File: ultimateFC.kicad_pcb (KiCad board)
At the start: 8 copper layers, 73 parts, among them J1 USB_B_Micro, U14 TPS62824ADMQ, U32 LMR33630CQRNX, U33 STM32H735VGH6, U36 ICM-20602, U37 S25FL064L, U39 BMP280, Y1 CSTNE8M00G550000R0

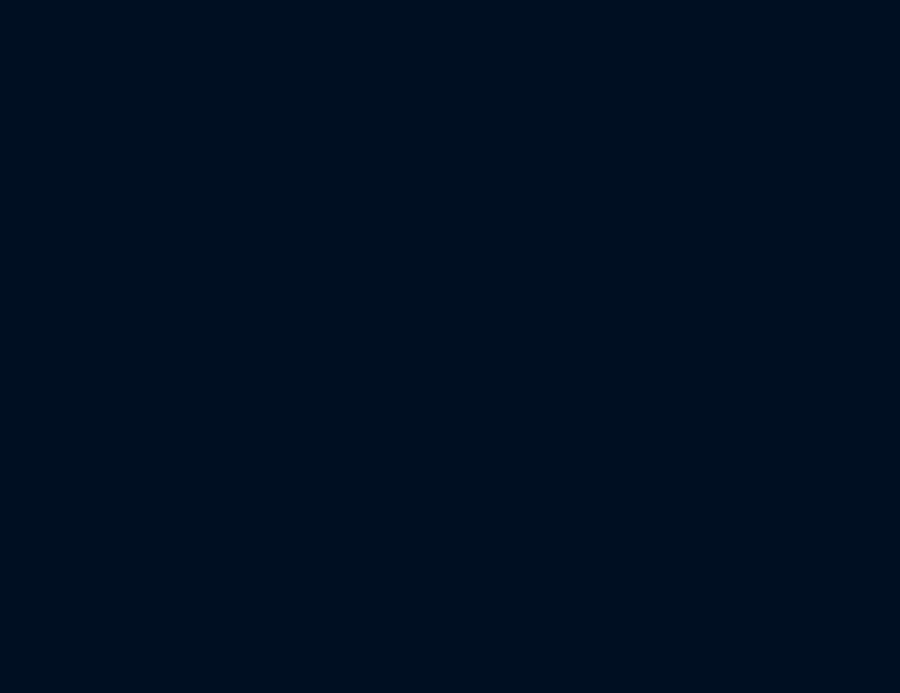
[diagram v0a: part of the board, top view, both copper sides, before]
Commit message: add HD DCDC
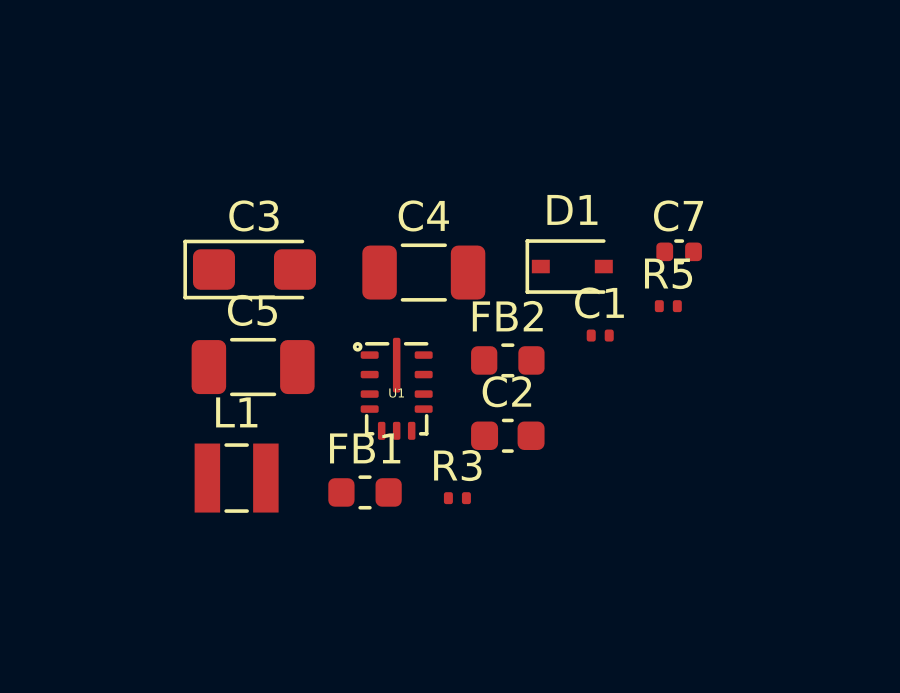
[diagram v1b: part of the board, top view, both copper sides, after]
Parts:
- added C1: 100nF, ultimateFC:C_0201_0603Metric_mod, F.Cu at (155.0, 115.0)
- added C2: 10µF, Capacitor_SMD:C_0603_1608Metric, F.Cu at (151.9, 118.3)
- added C3: 100µF, Capacitor_Tantalum_SMD:CP_EIA-3216-10_Kemet-I, F.Cu at (143.5, 112.8)
- added C4: 10µF, Capacitor_SMD:C_1206_3216Metric, F.Cu at (149.1, 112.9)
- added C5: 10µF, Capacitor_SMD:C_1206_3216Metric, F.Cu at (143.4, 116.0)
- added C7: 1µF, Capacitor_SMD:C_0402_1005Metric, F.Cu at (157.6, 112.2)
- added D1: PMEG3020EJ,115, Diode_SMD:D_SOD-323, F.Cu at (154.1, 112.7)
- added FB1: 120R@100Mhz, Inductor_SMD:L_0603_1608Metric, F.Cu at (147.2, 120.2)
- added FB2: 120R@100Mhz, Inductor_SMD:L_0603_1608Metric, F.Cu at (151.9, 115.8)
- added L1: 1µH, Inductor_SMD:L_Wuerth_MAPI-2506, F.Cu at (142.9, 119.8)
- added R3: 100k, ultimateFC:R_0201_0603Metric_mod, F.Cu at (150.2, 120.4)
- added R5: 11k, ultimateFC:R_0201_0603Metric_mod, F.Cu at (157.3, 114.0)
- added U1: LMR33620CRNXT, ultimateFC:Texas_RNX0012B, F.Cu at (148.2, 116.8)

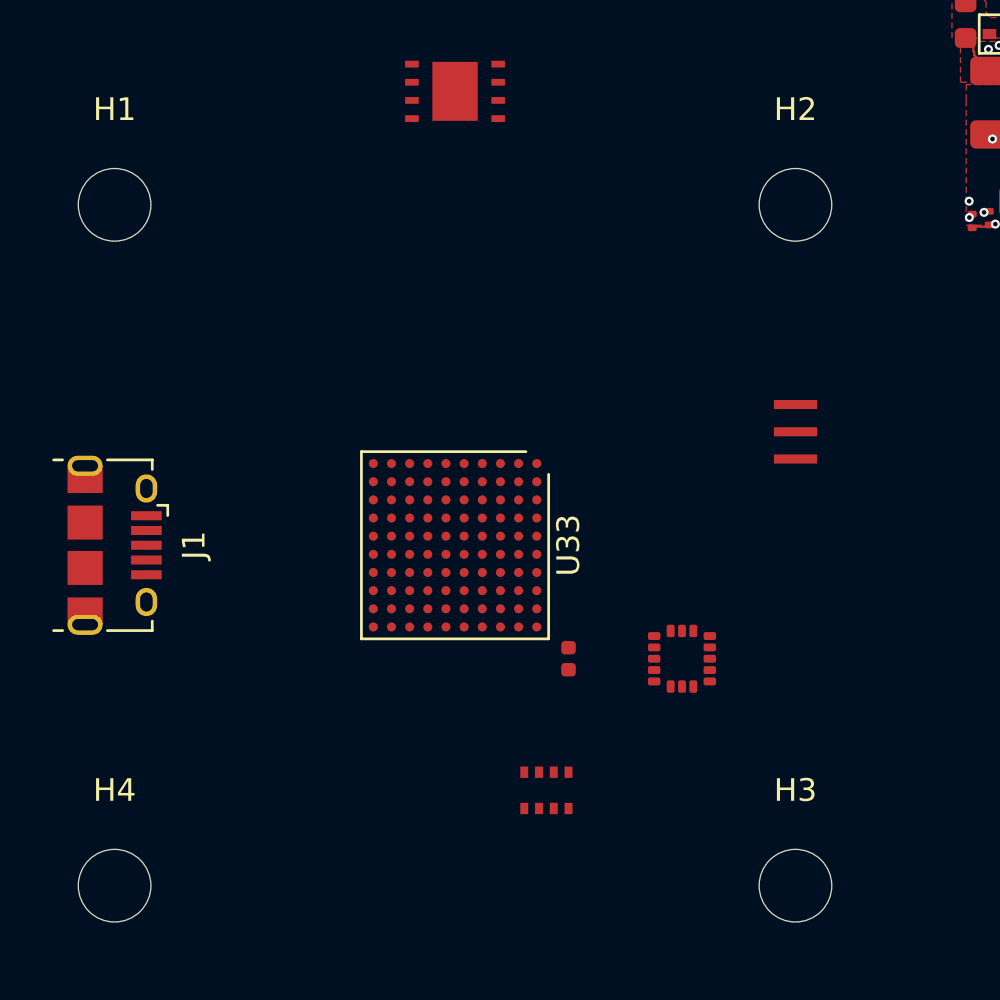
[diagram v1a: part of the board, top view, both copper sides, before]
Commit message: board edge
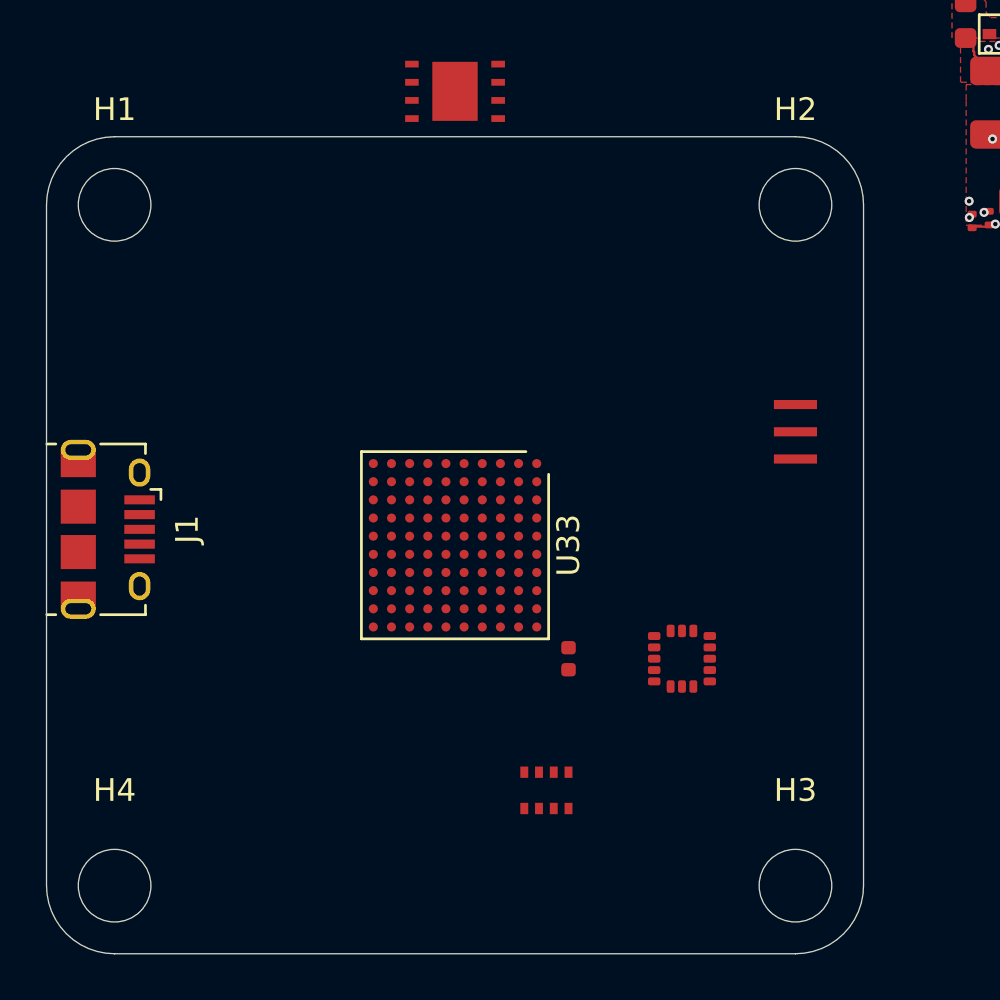
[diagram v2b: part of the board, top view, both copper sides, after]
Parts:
- moved J1 0.76 mm to (99.7, 114.3)
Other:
- board outline added: 36 x 36 mm
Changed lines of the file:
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@@
   )
   (footprint "Connector_USB:USB_Micro-B_Amphenol_10118194_Horizontal" (layer "F.Cu")
-    (at 100 115 -90)
+    (at 99.7 114.3 -90)
     (descr "USB Micro-B receptacle, horizontal, SMD, 10118194, https://cdn.amphenol-icc.com/media/wysiwyg/files/drawing/10118194.pdf")
     (tags "USB Micro B horizontal SMD")
@@
     ) (layer "F.SilkS") (width 0.1) (fill solid))
   (gr_circle (center 172.5 62) (end 170.4 62) (layer "F.SilkS") (width 0.12) (fill none))
+  (gr_circle (center 130 100) (end 133 100) (layer "Dwgs.User") (width 0.1) (fill none))
+  (gr_circle (center 100 100) (end 103 100) (layer "Dwgs.User") (width 0.1) (fill none))
+  (gr_circle (center 130 130) (end 133 130) (layer "Dwgs.User") (width 0.1) (fill none))
+  (gr_circle (center 100 130) (end 103 130) (layer "Dwgs.User") (width 0.1) (fill none))
   (gr_line (start 164.475 69.4) (end 167.65 69.45) (layer "Cmts.User") (width 0.05))
   (gr_line (start 189.15 87.275) (end 187 84.375) (layer "Cmts.User") (width 0.05))
@@
   (gr_line (start 197.825 72.65) (end 202.65 70.5) (layer "Cmts.User") (width 0.05))
   (gr_line (start 173.3 59.9) (end 176.525 56.375) (layer "Cmts.User") (width 0.05))
+  (gr_line (start 130 133) (end 100 133) (layer "Edge.Cuts") (width 0.05))
+  (gr_arc (start 130 97) (mid 132.12132 97.87868) (end 133 100) (layer "Edge.Cuts") (width 0.05))
+  (gr_arc (start 97 100) (mid 97.87868 97.87868) (end 100 97) (layer "Edge.Cuts") (width 0.05))
+  (gr_line (start 97 130) (end 97 100) (layer "Edge.Cuts") (width 0.05))
+  (gr_arc (start 100 133) (mid 97.87868 132.12132) (end 97 130) (layer "Edge.Cuts") (width 0.05))
+  (gr_line (start 133 100) (end 133 130) (layer "Edge.Cuts") (width 0.05))
+  (gr_line (start 100 97) (end 130 97) (layer "Edge.Cuts") (width 0.05))
+  (gr_arc (start 133 130) (mid 132.12132 132.12132) (end 130 133) (layer "Edge.Cuts") (width 0.05))
   (gr_text "Sideplating" (at 173.85 88.55) (layer "Cmts.User")
     (effects (font (size 0.8 0.8) (thickness 0.15)))

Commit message: update pcb layer count
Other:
- copper layers 8 -> 6
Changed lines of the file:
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@@
 (kicad_pcb (version 20211014) (generator pcbnew)
   (general
-    (thickness 1.2)
+    (thickness 1.15857)
   )
   (paper "A4")
   (layers
     (0 "F.Cu" signal)
-    (1 "In1.Cu" signal)
-    (2 "In2.Cu" signal)
-    (3 "In3.Cu" signal)
-    (4 "In4.Cu" signal)
-    (5 "In5.Cu" signal)
-    (6 "In6.Cu" signal)
+    (1 "In1.Cu" power "In1.Cu_Gnd")
+    (2 "In2.Cu" power "In2.Cu_3V3")
+    (3 "In3.Cu" power "In3.Cu_5V")
+    (4 "In4.Cu" power "In4.Cu_Gnd")
     (31 "B.Cu" signal)
     (32 "B.Adhes" user "B.Adhesive")
@@
   )
   (setup
+    (stackup
+      (layer "F.SilkS" (type "Top Silk Screen"))
+      (layer "F.Paste" (type "Top Solder Paste"))
+      (layer "F.Mask" (type "Top Solder Mask") (thickness 0.01))
+      (layer "F.Cu" (type "copper") (thickness 0.035))
+      (layer "dielectric 1" (type "core") (thickness 0.185714) (material "FR4") (epsilon_r 4.5) (loss_tangent 0.02))
+      (layer "In1.Cu" (type "copper") (thickness 0.035))
+      (layer "dielectric 2" (type "prepreg") (thickness 0.185714) (material "FR4") (epsilon_r 4.5) (loss_tangent 0.02))
+      (layer "In2.Cu" (type "copper") (thickness 0.035))
+      (layer "dielectric 3" (type "core") (thickness 0.185714) (material "FR4") (epsilon_r 4.5) (loss_tangent 0.02))
+      (layer "In3.Cu" (type "copper") (thickness 0.035))
+      (layer "dielectric 4" (type "prepreg") (thickness 0.185714) (material "FR4") (epsilon_r 4.5) (loss_tangent 0.02))
+      (layer "In4.Cu" (type "copper") (thickness 0.035))
+      (layer "dielectric 5" (type "core") (thickness 0.185714) (material "FR4") (epsilon_r 4.5) (loss_tangent 0.02))
+      (layer "B.Cu" (type "copper") (thickness 0.035))
+      (layer "B.Mask" (type "Bottom Solder Mask") (thickness 0.01))
+      (layer "B.Paste" (type "Bottom Solder Paste"))
+      (layer "B.SilkS" (type "Bottom Silk Screen"))
+      (copper_finish "None")
+      (dielectric_constraints no)
+    )
     (pad_to_mask_clearance 0.05)
     (solder_mask_min_width 0.1)

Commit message: added PADs.... lots of PADs
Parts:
- removed the C2 at (151.9, 118.3)
- removed the C22 at (174.7, 83.4)
- removed the C23 at (175.0, 80.4)
- removed the C24 at (179.0, 79.8)
- removed the C25 at (184.7, 74.7)
- removed the C27 at (169.8, 83.8)
- removed the D1 at (154.1, 112.7)
- added C31: 10µF, Capacitor_SMD:C_1206_3216Metric, F.Cu at (126.1, 123.1)
- added C33: 100µF, Capacitor_Tantalum_SMD:CP_EIA-3528-12_Kemet-T, F.Cu at (125.5, 130.8)
- added C34: 4.7µF, Capacitor_SMD:C_0402_1005Metric, F.Cu at (123.7, 131.9)
- added R12: 100R, ultimateFC:R_0201_0603Metric_mod, F.Cu at (106.2, 119.1)
- added R13: 100R, ultimateFC:R_0201_0603Metric_mod, B.Cu at (106.4, 128.5)
- added R14: 100R, ultimateFC:R_0201_0603Metric_mod, B.Cu at (104.6, 128.4)
- added R15: 100R, ultimateFC:R_0201_0603Metric_mod, F.Cu at (104.9, 116.4)
- added R16: 100R, ultimateFC:R_0201_0603Metric_mod, B.Cu at (108.4, 128.5)
- added R17: 100R, ultimateFC:R_0201_0603Metric_mod, F.Cu at (39.3, 136.7)
- added R18: 100R, ultimateFC:R_0201_0603Metric_mod, B.Cu at (118.8, 127.6)
- added R19: 100R, ultimateFC:R_0201_0603Metric_mod, B.Cu at (120.5, 128.5)
- added R20: 100R, ultimateFC:R_0201_0603Metric_mod, B.Cu at (118.3, 128.5)
- added R21: 100R, ultimateFC:R_0201_0603Metric_mod, B.Cu at (116.9, 127.6)
- added R23: 100R, ultimateFC:R_0201_0603Metric_mod, B.Cu at (122.5, 128.5)
- added TP1: Pad, TestPoint:TestPoint_Pad_1.5x1.5mm, F.Cu at (105.2, 98.3)
- added TP10: Pad, TestPoint:TestPoint_Pad_1.5x1.5mm, F.Cu at (101.5, 106.5)
- added TP100: Pad, TestPoint:TestPoint_Pad_1.5x1.5mm, F.Cu at (42.1, 130.6)
- added TP101: Pad, TestPoint:TestPoint_Pad_1.5x1.5mm, F.Cu at (62.0, 112.0)
- added TP102: Pad, TestPoint:TestPoint_Pad_1.5x1.5mm, F.Cu at (117.5, 105.2)
- added TP103: Pad, TestPoint:TestPoint_Pad_1.5x1.5mm, F.Cu at (113.5, 102.7)
- added TP104: Pad, TestPoint:TestPoint_Pad_1.5x1.5mm, F.Cu at (111.5, 105.2)
- added TP105: Pad, TestPoint:TestPoint_Pad_1.5x1.5mm, F.Cu at (111.5, 102.7)
- added TP106: Pad, TestPoint:TestPoint_Pad_1.5x1.5mm, F.Cu at (42.1, 119.9)
- added TP107: Pad, TestPoint:TestPoint_Pad_1.5x1.5mm, F.Cu at (109.5, 102.7)
- added TP108: Pad, TestPoint:TestPoint_Pad_1.5x1.5mm, F.Cu at (109.5, 105.2)
- added TP109: Pad, TestPoint:TestPoint_Pad_1.5x1.5mm, F.Cu at (107.5, 102.7)
- added TP11: Pad, TestPoint:TestPoint_Pad_1.5x1.5mm, F.Cu at (101.5, 108.5)
- added TP110: Pad, TestPoint:TestPoint_Pad_1.5x1.5mm, F.Cu at (107.5, 105.2)
- added TP12: Pad, TestPoint:TestPoint_Pad_1.5x1.5mm, F.Cu at (121.5, 107.2)
- added TP13: Pad, TestPoint:TestPoint_Pad_1.5x1.5mm, F.Cu at (121.5, 100.7)
- added TP14: Pad, TestPoint:TestPoint_Pad_1.5x1.5mm, F.Cu at (120.0, 131.7)
- added TP15: Pad, TestPoint:TestPoint_Pad_1.5x1.5mm, F.Cu at (122.1, 131.7)
- added TP16: Pad, TestPoint:TestPoint_Pad_1.5x1.5mm, F.Cu at (117.9, 131.7)
- added TP17: Pad, TestPoint:TestPoint_Pad_1.5x1.5mm, F.Cu at (115.8, 131.7)
- added TP18: Pad, TestPoint:TestPoint_Pad_1.5x1.5mm, F.Cu at (119.5, 100.7)
- added TP19: Pad, TestPoint:TestPoint_Pad_1.5x1.5mm, F.Cu at (119.5, 107.2)
- added TP2: Pad, TestPoint:TestPoint_Pad_1.5x1.5mm, F.Cu at (107.2, 98.3)
- added TP20: Pad, TestPoint:TestPoint_Pad_3.0x3.0mm, F.Cu at (131.0, 117.8)
- added TP21: Pad, TestPoint:TestPoint_Pad_3.0x3.0mm, F.Cu at (131.0, 114.0)
- added TP22: Pad, TestPoint:TestPoint_Pad_1.5x1.5mm, F.Cu at (106.6, 121.5)
- added TP23: Pad, TestPoint:TestPoint_Pad_1.5x1.5mm, F.Cu at (106.6, 128.0)
- added TP24: Pad, TestPoint:TestPoint_Pad_1.5x1.5mm, F.Cu at (104.6, 128.0)
- added TP25: Pad, TestPoint:TestPoint_Pad_1.5x1.5mm, F.Cu at (104.6, 121.5)
- added TP26: Pad, TestPoint:TestPoint_Pad_1.5x1.5mm, F.Cu at (108.6, 128.0)
- added TP27: Pad, TestPoint:TestPoint_Pad_1.5x1.5mm, F.Cu at (110.6, 128.0)
- added TP29: Pad, TestPoint:TestPoint_Pad_1.5x1.5mm, F.Cu at (118.6, 121.5)
- added TP3: Pad, TestPoint:TestPoint_Pad_1.5x1.5mm, F.Cu at (111.2, 98.3)
- added TP30: Pad, TestPoint:TestPoint_Pad_1.5x1.5mm, F.Cu at (120.6, 128.0)
- added TP31: Pad, TestPoint:TestPoint_Pad_1.5x1.5mm, F.Cu at (118.6, 128.0)
- added TP32: Pad, TestPoint:TestPoint_Pad_1.5x1.5mm, F.Cu at (116.6, 121.5)
- added TP33: Pad, TestPoint:TestPoint_Pad_1.5x1.5mm, F.Cu at (105.5, 102.7)
- added TP34: Pad, TestPoint:TestPoint_Pad_1.5x1.5mm, F.Cu at (56.3, 115.5)
- added TP35: Pad, TestPoint:TestPoint_Pad_1.5x1.5mm, F.Cu at (74.0, 115.5)
- added TP36: Pad, TestPoint:TestPoint_Pad_1.5x1.5mm, F.Cu at (49.2, 119.1)
- added TP37: Pad, TestPoint:TestPoint_Pad_1.5x1.5mm, F.Cu at (58.4, 112.0)
- added TP38: Pad, TestPoint:TestPoint_Pad_1.5x1.5mm, F.Cu at (69.6, 108.4)
- added TP39: Pad, TestPoint:TestPoint_Pad_1.5x1.5mm, F.Cu at (49.2, 129.8)
- added TP4: Pad, TestPoint:TestPoint_Pad_1.5x1.5mm, F.Cu at (109.2, 98.3)
- added TP40: Pad, TestPoint:TestPoint_Pad_1.5x1.5mm, F.Cu at (67.0, 119.1)
- added TP41: Pad, TestPoint:TestPoint_Pad_1.5x1.5mm, F.Cu at (123.5, 105.2)
- added TP42: Pad, TestPoint:TestPoint_Pad_1.5x1.5mm, F.Cu at (115.5, 105.2)
- added TP43: Pad, TestPoint:TestPoint_Pad_1.5x1.5mm, F.Cu at (99.5, 108.5)
- added TP44: Pad, TestPoint:TestPoint_Pad_1.5x1.5mm, F.Cu at (99.5, 106.5)
- added TP45: Pad, TestPoint:TestPoint_Pad_1.5x1.5mm, F.Cu at (104.6, 123.5)
- added TP46: Pad, TestPoint:TestPoint_Pad_1.5x1.5mm, F.Cu at (104.6, 126.0)
- added TP47: Pad, TestPoint:TestPoint_Pad_1.5x1.5mm, F.Cu at (106.6, 123.5)
- added TP48: Pad, TestPoint:TestPoint_Pad_1.5x1.5mm, F.Cu at (106.6, 126.0)
- added TP49: Pad, TestPoint:TestPoint_Pad_1.5x1.5mm, F.Cu at (70.5, 119.1)
- added TP5: Pad, TestPoint:TestPoint_Pad_1.5x1.5mm, F.Cu at (125.5, 98.5)
- added TP50: Pad, TestPoint:TestPoint_Pad_1.5x1.5mm, F.Cu at (122.6, 126.0)
- added TP51: Pad, TestPoint:TestPoint_Pad_1.5x1.5mm, F.Cu at (120.6, 123.5)
- added TP52: Pad, TestPoint:TestPoint_Pad_1.5x1.5mm, F.Cu at (122.6, 123.5)
- added TP53: Pad, TestPoint:TestPoint_Pad_1.5x1.5mm, F.Cu at (52.8, 108.5)
- added TP54: Pad, TestPoint:TestPoint_Pad_1.5x1.5mm, F.Cu at (47.8, 112.0)
- added TP55: Pad, TestPoint:TestPoint_Pad_1.5x1.5mm, F.Cu at (69.6, 110.4)
- added TP56: Pad, TestPoint:TestPoint_Pad_1.5x1.5mm, F.Cu at (45.6, 119.8)
- added TP57: Pad, TestPoint:TestPoint_Pad_1.5x1.5mm, F.Cu at (108.6, 126.0)
- added TP58: Pad, TestPoint:TestPoint_Pad_1.5x1.5mm, F.Cu at (70.5, 122.7)
- added TP59: Pad, TestPoint:TestPoint_Pad_1.5x1.5mm, F.Cu at (108.6, 123.5)
- added TP6: Pad, TestPoint:TestPoint_Pad_1.5x1.5mm, F.Cu at (98.5, 104.0)
- added TP60: Pad, TestPoint:TestPoint_Pad_1.5x1.5mm, F.Cu at (63.4, 133.3)
- added TP61: Pad, TestPoint:TestPoint_Pad_1.5x1.5mm, F.Cu at (110.6, 123.5)
- added TP62: Pad, TestPoint:TestPoint_Pad_1.5x1.5mm, F.Cu at (110.6, 126.0)
- added TP63: Pad, TestPoint:TestPoint_Pad_1.5x1.5mm, F.Cu at (56.4, 108.5)
- added TP64: Pad, TestPoint:TestPoint_Pad_1.5x1.5mm, F.Cu at (42.1, 123.5)
- added TP65: Pad, TestPoint:TestPoint_Pad_1.5x1.5mm, F.Cu at (112.1, 131.7)
- added TP66: Pad, TestPoint:TestPoint_Pad_1.5x1.5mm, F.Cu at (104.1, 131.7)
- added TP67: Pad, TestPoint:TestPoint_Pad_1.5x1.5mm, F.Cu at (106.1, 131.7)
- added TP68: Pad, TestPoint:TestPoint_Pad_1.5x1.5mm, F.Cu at (122.6, 128.0)
- added TP69: Pad, TestPoint:TestPoint_Pad_1.5x1.5mm, F.Cu at (108.6, 121.5)
- added TP7: Pad, TestPoint:TestPoint_Pad_1.5x1.5mm, F.Cu at (113.2, 98.3)
- added TP70: Pad, TestPoint:TestPoint_Pad_1.5x1.5mm, F.Cu at (38.5, 123.5)
- added TP71: Pad, TestPoint:TestPoint_Pad_1.5x1.5mm, F.Cu at (115.5, 102.7)
- added TP72: Pad, TestPoint:TestPoint_Pad_1.5x1.5mm, F.Cu at (113.5, 105.2)
- added TP73: Pad, TestPoint:TestPoint_Pad_1.5x1.5mm, F.Cu at (77.7, 108.5)
- added TP74: Pad, TestPoint:TestPoint_Pad_1.5x1.5mm, F.Cu at (49.2, 133.3)
- added TP75: Pad, TestPoint:TestPoint_Pad_1.5x1.5mm, F.Cu at (76.2, 112.0)
- added TP76: Pad, TestPoint:TestPoint_Pad_1.5x1.5mm, F.Cu at (105.5, 105.2)
- added TP77: Pad, TestPoint:TestPoint_Pad_1.5x1.5mm, F.Cu at (63.2, 127.0)
- added TP78: Pad, TestPoint:TestPoint_Pad_1.5x1.5mm, F.Cu at (112.6, 123.5)
- added TP79: Pad, TestPoint:TestPoint_Pad_1.5x1.5mm, F.Cu at (112.6, 126.0)
- added TP8: Pad, TestPoint:TestPoint_Pad_1.5x1.5mm, F.Cu at (115.2, 98.3)
- added TP80: Pad, TestPoint:TestPoint_Pad_1.5x1.5mm, F.Cu at (114.6, 123.5)
- added TP81: Pad, TestPoint:TestPoint_Pad_1.5x1.5mm, F.Cu at (118.6, 126.0)
- added TP82: Pad, TestPoint:TestPoint_Pad_1.5x1.5mm, F.Cu at (118.6, 123.5)
- added TP83: Pad, TestPoint:TestPoint_Pad_1.5x1.5mm, F.Cu at (120.6, 126.0)
- added TP84: Pad, TestPoint:TestPoint_Pad_1.5x1.5mm, F.Cu at (59.9, 129.8)
- added TP85: Pad, TestPoint:TestPoint_Pad_1.5x1.5mm, F.Cu at (117.5, 102.7)
- added TP86: Pad, TestPoint:TestPoint_Pad_1.5x1.5mm, F.Cu at (114.6, 126.0)
- added TP87: Pad, TestPoint:TestPoint_Pad_1.5x1.5mm, F.Cu at (116.6, 126.0)
- added TP88: Pad, TestPoint:TestPoint_Pad_1.5x1.5mm, F.Cu at (110.1, 131.7)
- added TP89: Pad, TestPoint:TestPoint_Pad_1.5x1.5mm, F.Cu at (108.1, 131.7)
- added TP9: Pad, TestPoint:TestPoint_Pad_1.5x1.5mm, F.Cu at (63.4, 119.1)
- added TP90: Pad, TestPoint:TestPoint_Pad_1.5x1.5mm, F.Cu at (116.6, 123.5)
- added TP91: Pad, TestPoint:TestPoint_Pad_1.5x1.5mm, F.Cu at (45.6, 130.4)
- added TP92: Pad, TestPoint:TestPoint_Pad_1.5x1.5mm, F.Cu at (58.0, 122.0)
- added TP93: Pad, TestPoint:TestPoint_Pad_1.5x1.5mm, F.Cu at (121.5, 105.2)
- added TP94: Pad, TestPoint:TestPoint_Pad_1.5x1.5mm, F.Cu at (123.5, 102.7)
- added TP95: Pad, TestPoint:TestPoint_Pad_1.5x1.5mm, F.Cu at (121.5, 102.7)
- added TP96: Pad, TestPoint:TestPoint_Pad_1.5x1.5mm, F.Cu at (119.5, 105.2)
- added TP97: Pad, TestPoint:TestPoint_Pad_1.5x1.5mm, F.Cu at (119.5, 102.7)
- added TP98: Pad, TestPoint:TestPoint_Pad_1.5x1.5mm, F.Cu at (56.3, 126.2)
- added TP99: Pad, TestPoint:TestPoint_Pad_1.5x1.5mm, F.Cu at (56.3, 119.1)
- added U6: BMI270, Package_LGA:Bosch_LGA-14_3x2.5mm_P0.5mm, F.Cu at (107.2, 117.0)
- C10: renamed from C15; value 2.2µF -> 4.7µF; footprint ultimateFC:C_AVX_Super_Low_ESL -> Capacitor_SMD:C_0402_1005Metric
- C12: renamed from C20; value 1µF -> 4.7µF; footprint ultimateFC:C_AVX_Super_Low_ESL -> Capacitor_SMD:C_0402_1005Metric
- C13: renamed from C21; value 2.2µF -> 4.7µF; footprint ultimateFC:C_AVX_Super_Low_ESL -> Capacitor_SMD:C_0402_1005Metric
- C14: renamed from C41; value 1µF -> 4.7µF; footprint ultimateFC:C_AVX_Super_Low_ESL -> Capacitor_SMD:C_0402_1005Metric
- C15: renamed from C42; value 2.2µF -> 4.7µF; footprint ultimateFC:C_AVX_Super_Low_ESL -> Capacitor_SMD:C_0402_1005Metric
- C16: renamed from C43; value 1µF -> 4.7µF; footprint ultimateFC:C_AVX_Super_Low_ESL -> Capacitor_SMD:C_0402_1005Metric
- C17: renamed from C44; value 2.2µF -> 4.7µF; footprint ultimateFC:C_AVX_Super_Low_ESL -> Capacitor_SMD:C_0402_1005Metric
- C29: renamed from C7; footprint Capacitor_SMD:C_0402_1005Metric -> ultimateFC:C_0201_0603Metric_mod
- C3: renamed from C37; footprint Capacitor_SMD:C_0402_1005Metric -> ultimateFC:C_0201_0603Metric_mod
- C32: renamed from C3; footprint Capacitor_Tantalum_SMD:CP_EIA-3216-10_Kemet-I -> Capacitor_Tantalum_SMD:CP_EIA-3528-12_Kemet-T
- C35: renamed from C52; value 2.2µF -> 4.7µF
- C36: renamed from C50; value 2.2µF -> 4.7µF
- C38: renamed from C51; value 2.2µF -> 4.7µF
- C9: renamed from C14; value 1µF -> 4.7µF; footprint ultimateFC:C_AVX_Super_Low_ESL -> Capacitor_SMD:C_0402_1005Metric
- H1: renamed from H3; footprint MountingHole:MountingHole_3.2mm_M3 -> MountingHole:MountingHole_3.2mm_M3_DIN965_Pad
- H2: renamed from H1; footprint MountingHole:MountingHole_3.2mm_M3 -> MountingHole:MountingHole_3.2mm_M3_DIN965_Pad
- H3: renamed from H2; footprint MountingHole:MountingHole_3.2mm_M3 -> MountingHole:MountingHole_3.2mm_M3_DIN965_Pad
- H4: footprint MountingHole:MountingHole_3.2mm_M3 -> MountingHole:MountingHole_3.2mm_M3_DIN965_Pad
- moved C23 47.5 mm to (99.0, 126.2)
- moved FB3 46.6 mm to (100.4, 119.4)
- moved R3 46.3 mm to (99.0, 125.6), turned to 180 degrees
- moved L2 46.2 mm to (100.8, 122.0)
- moved C11 46.2 mm to (98.7, 120.7)
- moved C24 46.2 mm to (98.8, 123.4)
- moved C26 46.2 mm to (98.9, 124.6)
- moved U2 46.2 mm to (99.0, 122.1)
- moved R4 46.2 mm to (97.7, 122.2)
- moved FB4 45.7 mm to (100.8, 125.2), turned to 90 degrees
- moved R7 35.4 mm to (104.0, 108.5), turned to 0 degrees
- moved R8 34.5 mm to (104.0, 107.5), turned to 0 degrees
- moved FB6 28.8 mm to (125.8, 127.8)
- moved R10 27.5 mm to (130.4, 119.9)
- moved C29 27.2 mm to (131.5, 119.9), turned to 180 degrees
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- renumbered C35 to C1, C6 to C11, C55 to C18, C45 to C19, C36 to C2, C56 to C20, C46 to C21, C26 to C22, C53 to C23, C11 to C24, C28 to C25, C8 to C26, C4 to C27, C5 to C28, C1 to C30, C57 to C37, C38 to C4, C39 to C5, C40 to C6, C12 to C7, C13 to C8, D101 to D1, D3 to D2, D4 to D3, D2 to D4, FB5 to FB1, FB6 to FB2, FB1 to FB5, FB2 to FB6, L3 to L1, L1 to L3, L5 to L4, R5 to R10, R30 to R11, R4 to R22, R9 to R24, R10 to R25, R7 to R26, R8 to R27, R21 to R3, R22 to R4, R47 to R5, R48 to R6, R36 to R7, R37 to R8, R3 to R9, TP29 to TP28, U32 to U1, U14 to U2, U1 to U3, U37 to U4, U39 to U5, U33 to U7, U36 to U8
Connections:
- C25 pad 1: vol_sig -> Net-(C25-Pad1)
- C36 pad 1: Net-(C50-Pad1) -> Net-(C36-Pad1)
- C37 pad 1: Net-(C50-Pad1) -> Net-(C36-Pad1)
- C38 pad 1: Net-(C50-Pad1) -> Net-(C36-Pad1)
- FB5 pad 1: Net-(D1-Pad1) (its old number) -> +BATT
- L4 pad 2: Net-(C50-Pad1) -> Net-(C36-Pad1)
- R24 pad 1: UC_LED_1 -> Net-(R24-Pad1)
- R25 pad 1: UC_LED_2 -> Net-(R25-Pad1)
- R5 pad 2: vol_sig -> Net-(C25-Pad1)
- R6 pad 1: vol_sig -> Net-(C25-Pad1)
- R7 pad 2: I2C_SDA -> Net-(R7-Pad2)
- R8 pad 2: I2C_SCL -> Net-(R8-Pad2)
- U4 pad 1: CS_FLASH -> Net-(U4-Pad1)
- U4 pad 2: MISO_FLASH -> Net-(U4-Pad2)
- U4 pad 5: MOSI_FLASH -> Net-(U4-Pad5)
- U4 pad 6: SCLK_FLASH -> Net-(U4-Pad6)
- U5 pad 3: I2C_SDA -> Net-(R7-Pad2)
- U5 pad 4: I2C_SCL -> Net-(R8-Pad2)
- U7 pad A4: unconnected-(U33-PadA4) -> Net-(U7-PadA4)
- U7 pad A6: unconnected-(U33-PadA6) -> Net-(U7-PadA6)
- U7 pad A8: unconnected-(U33-PadA8) -> Net-(U7-PadA8)
- U7 pad B1: unconnected-(U33-PadB1) -> Net-(U7-PadB1)
- U7 pad B2: unconnected-(U33-PadB2) -> Net-(U7-PadB2)
- U7 pad B3: unconnected-(U33-PadB3) -> Net-(U7-PadB3)
- U7 pad B6: unconnected-(U33-PadB6) -> Net-(U7-PadB6)
- U7 pad B7: unconnected-(U33-PadB7) -> Net-(U7-PadB7)
- U7 pad B8: unconnected-(U33-PadB8) -> Net-(U7-PadB8)
- U7 pad C10: INT_GYRO -> /SWDIO
- U7 pad C5: unconnected-(U33-PadC5) -> Net-(U7-PadC5)
- U7 pad C6: unconnected-(U33-PadC6) -> Net-(U7-PadC6)
- U7 pad C7: unconnected-(U33-PadC7) -> Net-(U7-PadC7)
- U7 pad C9: unconnected-(U33-PadC9) -> /SWDCLK
- U7 pad D8: Net-(C50-Pad1) -> Net-(C36-Pad1)
- U7 pad E10: unconnected-(U33-PadE10) -> Net-(U7-PadE10)
- U7 pad E2: Net-(C50-Pad1) -> Net-(C36-Pad1)
- U7 pad E3: unconnected-(U33-PadE3) -> Net-(U7-PadE3)
- U7 pad E4: unconnected-(U33-PadE4) -> Net-(U7-PadE4)
- U7 pad E6: Net-(C50-Pad1) -> Net-(C36-Pad1)
- U7 pad F1: unconnected-(U33-PadF1) -> Net-(U7-PadF1)
- U7 pad F10: unconnected-(U33-PadF10) -> Net-(U7-PadF10)
- U7 pad F3: unconnected-(U33-PadF3) -> Net-(U7-PadF3)
- U7 pad F4: unconnected-(U33-PadF4) -> Net-(U7-PadF4)
- U7 pad F7: +3V3 -> Net-(C36-Pad1)
- U7 pad G4: unconnected-(U33-PadG4) -> Net-(U7-PadG4)
- U7 pad G6: Net-(C50-Pad1) -> Net-(C36-Pad1)
- U7 pad H4: unconnected-(U33-PadH4) -> Net-(U7-PadH4)
- U7 pad H6: unconnected-(U33-PadH6) -> Net-(U7-PadH6)
- U7 pad H7: unconnected-(U33-PadH7) -> Net-(U7-PadH7)
- U7 pad J5: unconnected-(U33-PadJ5) -> Net-(U7-PadJ5)
- U7 pad K1: unconnected-(U33-PadK1) -> Net-(U7-PadK1)
- U7 pad K6: unconnected-(U33-PadK6) -> Net-(U7-PadK6)
- U8 pad 2: SCLK_GYRO -> Net-(U8-Pad2)
- U8 pad 3: MOSI_GYRO -> Net-(U8-Pad3)
- U8 pad 4: MISO_GYRO -> Net-(U8-Pad4)
- U8 pad 5: CS_GYRO -> Net-(U8-Pad5)
- U8 pad 6: INT_GYRO -> Net-(U8-Pad6)
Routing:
- net +3V3: track 1.12 -> 6.31 mm, vias 5 -> 7
- net Net-(C36-Pad1): track 0.00 -> 4.19 mm
- net GND: track 12.4 -> 13.6 mm, vias 35 -> 26
- net Net-(C1-Pad1): track 9.69 -> 8.96 mm
- net Net-(C24-Pad1): track 0.58 -> 0.00 mm
- net +BATT: track 0.52 -> 0.00 mm, vias 2 -> 0
- net Net-(C23-Pad2): track 1.22 -> 0.98 mm, vias 2 -> 1
- net I2C_SDA: track 0.24 -> 0.00 mm, vias 1 -> 0
- net +5V: track 1.63 -> 1.70 mm, vias 10 -> 3
- net Net-(C5-Pad1): vias 2 -> 1
- net Net-(R26-Pad2): vias 1 -> 0
- net I2C_SCL: vias 1 -> 0
- added copper zone on F.Cu, net Net-(C35-Pad1)
- removed copper zone on F.Cu, net +3V3
- removed copper zone on F.Cu, net Net-(C1-Pad1)
- removed copper zone on F.Cu, net Net-(C24-Pad1)
- removed copper zone on F.Cu, net Net-(D1-Pad1)

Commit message: schematic and layout update
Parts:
- added R28: 14k, Resistor_SMD:R_0402_1005Metric, F.Cu at (142.6, 116.7)
- added TP111: bridge, ultimateFC:solderbridge_tiny, B.Cu at (145.1, 116.7)
- C23, C25, C29, C3, C30, C4: footprint ultimateFC:C_0201_0603Metric_mod -> Capacitor_SMD:C_0402_1005Metric
- C36, C37, C38, L4, TP10, TP11, TP12, TP13, TP18, TP19, TP22, TP23, TP24, TP25, TP26, TP27, TP29, TP30, TP31, TP32, TP43, TP44, TP45, TP46, TP47, TP48, TP51, TP59, TP68, TP69, TP70, TP81, TP82, TP83, TP90, TP93, TP95, TP96, TP97: moved to B.Cu
- D2, D3: footprint LED_SMD:LED_0201_0603Metric -> LED_SMD:LED_0402_1005Metric
- R1, R10, R11, R12, R15, R17, R2, R22, R24, R25, R26, R27, R3, R4, R6, R7, R8, R9: footprint ultimateFC:R_0201_0603Metric_mod -> Resistor_SMD:R_0402_1005Metric
- R13, R14, R16, R18, R19, R20, R21, R23: footprint ultimateFC:R_0201_0603Metric_mod -> Resistor_SMD:R_0402_1005Metric; moved to F.Cu
- U5: value BMP280 -> DPS310
- moved TP70 99.6 mm to (136.8, 139.7), turned to 180 degrees
- moved C37 78.0 mm to (112.2, 113.5), turned to 180 degrees
- moved C36 77.1 mm to (112.2, 114.5), turned to 180 degrees
- moved R26 77.1 mm to (102.6, 115.5), turned to 90 degrees
- moved R17 71.5 mm to (105.9, 110.7), turned to -90 degrees
- moved C38 71.4 mm to (112.2, 112.6), turned to 180 degrees
- moved R27 71.3 mm to (102.6, 113.6), turned to 90 degrees
- moved L4 69.9 mm to (113.6, 111.4), turned to 180 degrees
- moved TP77 41.2 mm to (103.4, 136.2)
- moved TP59 35.3 mm to (138.8, 141.7), turned to 180 degrees
- moved TP69 35.3 mm to (138.8, 139.7), turned to 180 degrees
- moved TP18 33.9 mm to (143.5, 124.6), turned to 180 degrees
- moved TP19 33.9 mm to (143.5, 131.1), turned to 180 degrees
- moved TP96 33.9 mm to (143.5, 129.1), turned to 180 degrees
- moved TP97 33.9 mm to (143.5, 126.6), turned to 180 degrees
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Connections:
- net Net-(R12-Pad1) renamed /MISO_270
- net Net-(R13-Pad1) renamed /MOSI_270
- net Net-(R14-Pad1) renamed /SCK_270
- net Net-(R15-Pad1) renamed /CS_270
- net Net-(R16-Pad1) renamed /INT1_270
- net Net-(R17-Pad1) renamed /INT2_270
- net Net-(R18-Pad1) renamed /MISO_20602
- net Net-(R19-Pad1) renamed /MOSI_20602
- net Net-(R20-Pad1) renamed /SCK_20602
- net Net-(R21-Pad1) renamed /CS_20602
- net Net-(R23-Pad2) renamed /INT_20602
- net Net-(R24-Pad1) renamed /A_LED_BL
- net Net-(R25-Pad1) renamed /A_LED_WT
- net Net-(R7-Pad2) renamed /SCL_DPS
- net Net-(R8-Pad2) renamed /SCK_DPS
- net Net-(U4-Pad1) renamed /CS_FLASH_IC
- net Net-(U4-Pad2) renamed /MISO_FLASH_IC
- net Net-(U4-Pad5) renamed /MOSI_FLASH_IC
- net Net-(U4-Pad6) renamed /SCK_FLASH_IC
- R10 pad 2: GND -> Net-(R10-Pad2)
- R26 pad 2: Net-(R26-Pad2) -> /USB_VBUS_sense
- R27 pad 1: Net-(R26-Pad2) -> /USB_VBUS_sense
- TP100 pad 1: Net-(U7-PadK6) -> Net-(TP100-Pad1)
- TP101 pad 1: Net-(U7-PadH6) -> Net-(TP101-Pad1)
- TP102 pad 1: Net-(U7-PadB2) -> Net-(TP102-Pad1)
- TP107 pad 1: Net-(U7-PadK1) -> Net-(TP107-Pad1)
- TP35 pad 1: Net-(U7-PadJ5) -> Net-(TP35-Pad1)
- TP36 pad 1: Net-(U7-PadB6) -> Net-(TP36-Pad1)
- TP37 pad 1: Net-(U7-PadC5) -> Net-(TP37-Pad1)
- TP38 pad 1: Net-(U7-PadA6) -> Net-(TP38-Pad1)
- TP41 pad 1: Net-(U7-PadA4) -> Net-(TP41-Pad1)
- TP42 pad 1: Net-(U7-PadE3) -> Net-(TP42-Pad1)
- TP49 pad 1: Net-(U7-PadC7) -> Net-(TP49-Pad1)
- TP50 pad 1: Net-(U7-PadB8) -> Net-(TP50-Pad1)
- TP52 pad 1: Net-(U7-PadA8) -> Net-(TP52-Pad1)
- TP53 pad 1: Net-(U7-PadB7) -> Net-(TP53-Pad1)
- TP56 pad 1: Net-(U7-PadC6) -> Net-(TP56-Pad1)
- TP60 pad 1: Net-(U7-PadH7) -> Net-(TP60-Pad1)
- TP71 pad 1: Net-(U7-PadF3) -> Net-(TP71-Pad1)
- TP72 pad 1: Net-(U7-PadF1) -> Net-(TP72-Pad1)
- TP73 pad 1: Net-(U7-PadF4) -> Net-(TP73-Pad1)
- TP74 pad 1: Net-(U7-PadG4) -> Net-(TP74-Pad1)
- TP75 pad 1: Net-(U7-PadH4) -> Net-(TP75-Pad1)
- TP84 pad 1: Net-(U7-PadE4) -> Net-(TP84-Pad1)
- TP85 pad 1: Net-(U7-PadB1) -> Net-(TP85-Pad1)
- TP86 pad 1: Net-(U7-PadF10) -> Net-(TP86-Pad1)
- TP87 pad 1: Net-(U7-PadE10) -> Net-(TP87-Pad1)
- TP94 pad 1: Net-(U7-PadB3) -> Net-(TP94-Pad1)
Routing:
- net Net-(J1-Pad3): track 0.00 -> 11.4 mm
- net Net-(J1-Pad2): track 0.00 -> 10.5 mm
- net SCLK_GYRO: track 0.00 -> 9.38 mm, vias 0 -> 1
- net Net-(R12-Pad2): track 0.00 -> 6.97 mm
- net Net-(R13-Pad2): track 0.00 -> 4.71 mm
- net MOSI_GYRO: track 0.00 -> 4.48 mm, vias 0 -> 1
- net Net-(R16-Pad2): track 0.00 -> 4.46 mm
- net MISO_GYRO: track 0.00 -> 4.35 mm, vias 0 -> 1
- net OSC_OUT: track 0.00 -> 3.78 mm
- net Net-(R14-Pad2): track 0.00 -> 3.29 mm
- net GND: track 13.6 -> 16.9 mm, vias 26 -> 29
- net Net-(R15-Pad2): track 0.00 -> 2.87 mm
- net Net-(U7-PadG1): track 0.00 -> 2.81 mm
- net +5V: track 1.70 -> 0.00 mm, vias 3 -> 2
- net Net-(R17-Pad2): track 0.00 -> 1.49 mm
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- added copper zone on F.Cu, net Net-(C23-Pad1)
- removed copper zone on F.Cu, net +5V
